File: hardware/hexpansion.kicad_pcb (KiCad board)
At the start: 2 copper layers, 86.8 x 46 mm, 97 parts, among them J1 Hexpansion-Connector, J2 Conn_01x03_Pin, SW1 SKTAACE010, SW2 SKTAACE010, U1 MT3608, U10 XL-0807RGBC-WS2812B-S, U11 XL-0807RGBC-WS2812B-S, U12 XL-0807RGBC-WS2812B-S, U13 XL-0807RGBC-WS2812B-S, U14 XL-0807RGBC-WS2812B-S, U15 XL-0807RGBC-WS2812B-S, U16 XL-0807RGBC-WS2812B-S, U17 XL-0807RGBC-WS2812B-S, U18 XL-0807RGBC-WS2812B-S, U19 XL-0807RGBC-WS2812B-S, U2 ZD24C64A-XGMT, U20 XL-0807RGBC-WS2812B-S, U21 XL-0807RGBC-WS2812B-S, U22 XL-0807RGBC-WS2812B-S, U23 XL-0807RGBC-WS2812B-S, U24 XL-0807RGBC-WS2812B-S, U25 XL-0807RGBC-WS2812B-S, U26 XL-0807RGBC-WS2812B-S, U27 XL-0807RGBC-WS2812B-S, U28 XL-0807RGBC-WS2812B-S, U29 XL-0807RGBC-WS2812B-S, U3 XL-0807RGBC-WS2812B-S, U30 XL-0807RGBC-WS2812B-S, U31 XL-0807RGBC-WS2812B-S, U32 XL-0807RGBC-WS2812B-S, U33 XL-0807RGBC-WS2812B-S, U34 XL-0807RGBC-WS2812B-S, U35 XL-0807RGBC-WS2812B-S, U36 XL-0807RGBC-WS2812B-S, U37 XL-0807RGBC-WS2812B-S, U38 XL-0807RGBC-WS2812B-S, U39 XL-0807RGBC-WS2812B-S, U4 XL-0807RGBC-WS2812B-S, U40 XL-0807RGBC-WS2812B-S, U41 XL-0807RGBC-WS2812B-S, U42 XL-0807RGBC-WS2812B-S, U43 XL-0807RGBC-WS2812B-S, U44 XL-0807RGBC-WS2812B-S, U45 XL-0807RGBC-WS2812B-S, U46 XL-0807RGBC-WS2812B-S, U47 XL-0807RGBC-WS2812B-S, U48 XL-0807RGBC-WS2812B-S, U49 XL-0807RGBC-WS2812B-S, U5 XL-0807RGBC-WS2812B-S, U50 XL-0807RGBC-WS2812B-S, U51 XL-0807RGBC-WS2812B-S, U52 XL-0807RGBC-WS2812B-S, U53 XL-0807RGBC-WS2812B-S, U54 XL-0807RGBC-WS2812B-S, U55 XL-0807RGBC-WS2812B-S, U56 XL-0807RGBC-WS2812B-S, U57 XL-0807RGBC-WS2812B-S, U58 XL-0807RGBC-WS2812B-S, U59 XL-0807RGBC-WS2812B-S, U6 XL-0807RGBC-WS2812B-S, U60 XL-0807RGBC-WS2812B-S, U61 XL-0807RGBC-WS2812B-S, U62 XL-0807RGBC-WS2812B-S, U63 XL-0807RGBC-WS2812B-S, U64 XL-0807RGBC-WS2812B-S, U65 XL-0807RGBC-WS2812B-S, U66 XL-0807RGBC-WS2812B-S, U67 XL-0807RGBC-WS2812B-S, U68 XL-0807RGBC-WS2812B-S, U69 XL-0807RGBC-WS2812B-S, U7 XL-0807RGBC-WS2812B-S, U70 XL-0807RGBC-WS2812B-S, U71 XL-0807RGBC-WS2812B-S, U72 XL-0807RGBC-WS2812B-S, U73 XL-0807RGBC-WS2812B-S, U74 XL-0807RGBC-WS2812B-S, U75 XL-0807RGBC-WS2812B-S, U76 XL-0807RGBC-WS2812B-S, U77 XL-0807RGBC-WS2812B-S, U78 XL-0807RGBC-WS2812B-S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

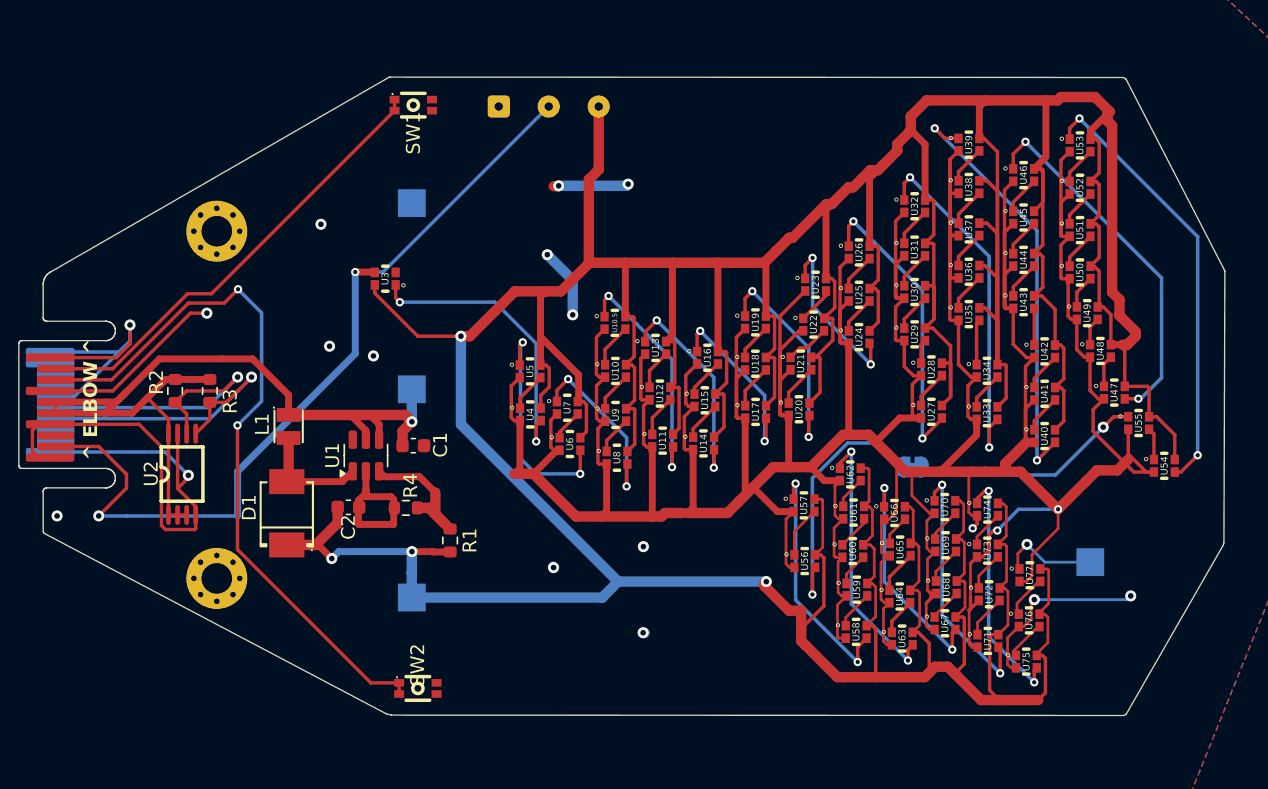
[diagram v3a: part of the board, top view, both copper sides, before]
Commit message: Update silkscreen and add some more ground ties
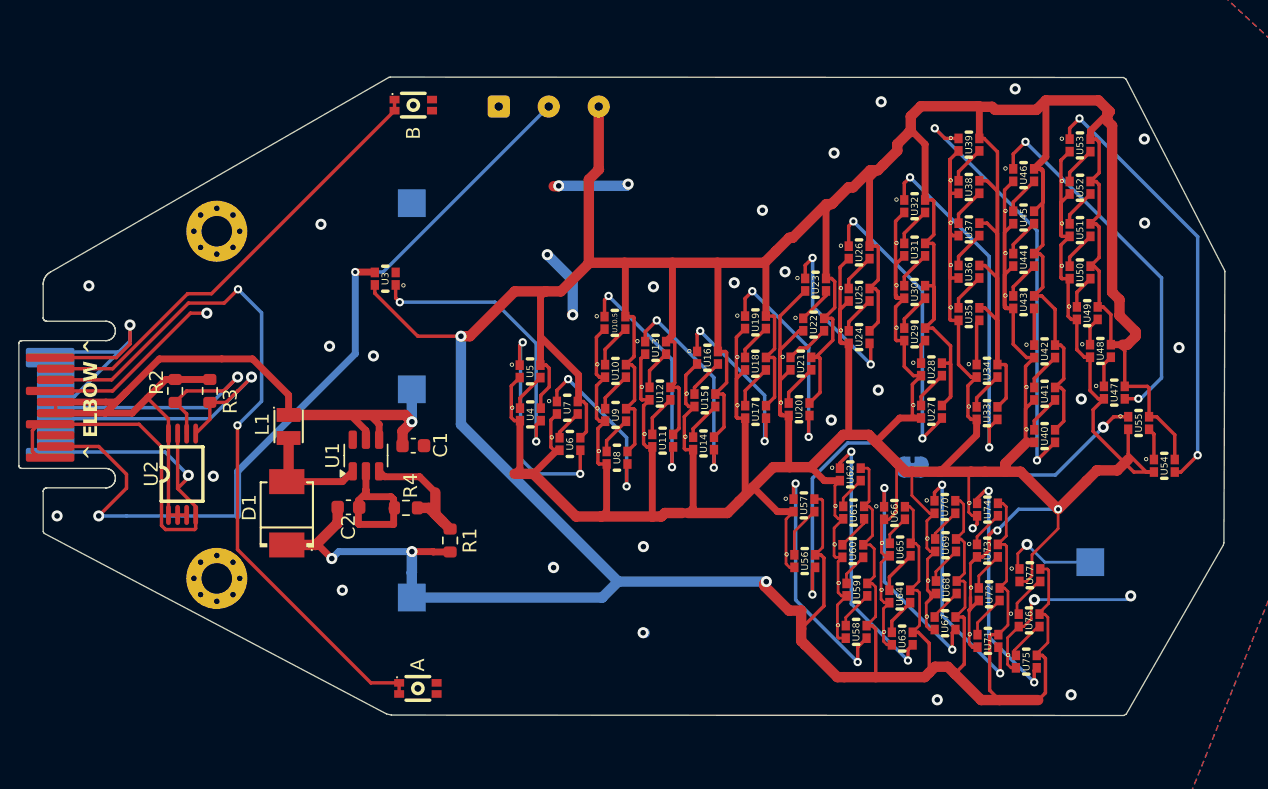
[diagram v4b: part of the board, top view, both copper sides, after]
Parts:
- Data Out: renamed from TP3
- renumbered TP1 to 3.3V, TP2 to 5V, SW2 to A, SW1 to B, TP4 to GND
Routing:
- net +5V: track 541.6 -> 541.0 mm
- net /GND: vias 19 -> 37
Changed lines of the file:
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@@
 		(layer "F.Cu")
 		(at 126.98 120.42)
-		(property "Reference" "SW2"
+		(property "Reference" "A"
 			(at -0.01 -1.69 90)
 			(layer "F.SilkS")
@@
 		(layer "F.Cu")
 		(at 126.65 78.42)
-		(property "Reference" "SW1"
+		(property "Reference" "B"
 			(at 0.01 2.01 90)
 			(layer "F.SilkS")
@@
 		(descr "SMD rectangular pad as test Point, square 2.0mm side length")
 		(tags "test point SMD pad rectangle square")
-		(property "Reference" "TP4"
+		(property "Reference" "GND"
 			(at 0 1.998 90)
 			(layer "B.SilkS")
@@
 		(descr "SMD rectangular pad as test Point, square 2.0mm side length")
 		(tags "test point SMD pad rectangle square")
-		(property "Reference" "TP1"
+		(property "Reference" "3.3V"
 			(at 0 1.998 90)
 			(layer "B.SilkS")
@@
 		(descr "SMD rectangular pad as test Point, square 2.0mm side length")
 		(tags "test point SMD pad rectangle square")
-		(property "Reference" "TP2"
+		(property "Reference" "5V"
 			(at 0 1.998 90)
 			(layer "B.SilkS")
@@
 		(descr "SMD rectangular pad as test Point, square 2.0mm side length")
 		(tags "test point SMD pad rectangle square")
-		(property "Reference" "TP3"
+		(property "Reference" "Data Out"
 			(at 0 1.998 90)
 			(layer "B.SilkS")
@@
 	)
 	(via
+		(at 151.79 85.99)
+		(size 0.8)
+		(drill 0.4)
+		(layers "F.Cu" "B.Cu")
+		(free yes)
+		(net 1)
+	)
+	(via
 		(at 173.08 107.52)
 		(size 0.6)
@@
 	)
 	(via
+		(at 103.29 91.43)
+		(size 0.8)
+		(drill 0.4)
+		(layers "F.Cu" "B.Cu")
+		(free yes)
+		(net 1)
+	)
+	(via
+		(at 149.76 91.21)
+		(size 0.8)
+		(drill 0.4)
+		(layers "F.Cu" "B.Cu")
+		(free yes)
+		(net 1)
+	)
+	(via
 		(at 120 87)
 		(size 0.8)
@@
 	)
 	(via
+		(at 156.75 101.1)
+		(size 0.8)
+		(drill 0.4)
+		(layers "F.Cu" "B.Cu")
+		(free yes)
+		(net 1)
+	)
+	(via
+		(at 156.95 81.87)
+		(size 0.8)
+		(drill 0.4)
+		(layers "F.Cu" "B.Cu")
+		(free yes)
+		(net 1)
+	)
+	(via
+		(at 174.02 120.88)
+		(size 0.8)
+		(drill 0.4)
+		(layers "F.Cu" "B.Cu")
+		(free yes)
+		(net 1)
+	)
+	(via
+		(at 179.29 80.86)
+		(size 0.8)
+		(drill 0.4)
+		(layers "F.Cu" "B.Cu")
+		(free yes)
+		(net 1)
+	)
+	(via
+		(at 169.99 77.25)
+		(size 0.8)
+		(drill 0.4)
+		(layers "F.Cu" "B.Cu")
+		(free yes)
+		(net 1)
+	)
+	(via
+		(at 143.94 91.5)
+		(size 0.8)
+		(drill 0.4)
+		(layers "F.Cu" "B.Cu")
+		(free yes)
+		(net 1)
+	)
+	(via
 		(at 136.3 89.19)
 		(size 0.8)
@@
 	)
 	(via
+		(at 174.75 99.58)
+		(size 0.8)
+		(drill 0.4)
+		(layers "F.Cu" "B.Cu")
+		(free yes)
+		(net 1)
+	)
+	(via
+		(at 121.54 113.35)
+		(size 0.8)
+		(drill 0.4)
+		(layers "F.Cu" "B.Cu")
+		(free yes)
+		(net 1)
+	)
+	(via
+		(at 160.13 98.94)
+		(size 0.8)
+		(drill 0.4)
+		(layers "F.Cu" "B.Cu")
+		(free yes)
+		(net 1)
+	)
+	(via
 		(at 166.93 108.89)
 		(size 0.6)
@@
 	)
 	(via
+		(at 179.31 86.91)
+		(size 0.8)
+		(drill 0.4)
+		(layers "F.Cu" "B.Cu")
+		(free yes)
+		(net 1)
+	)
+	(via
 		(at 168.705 109.05)
 		(size 0.6)
@@
 	)
 	(via
+		(at 153.42 90.42)
+		(size 0.8)
+		(drill 0.4)
+		(layers "F.Cu" "B.Cu")
+		(free yes)
+		(net 1)
+	)
+	(via
+		(at 112.25 105.14)
+		(size 0.8)
+		(drill 0.4)
+		(layers "F.Cu" "B.Cu")
+		(free yes)
+		(net 1)
+	)
+	(via
 		(at 111.785214 93.40067)
 		(size 0.8)
@@
 	)
 	(via
+		(at 181.79 95.88)
+		(size 0.8)
+		(drill 0.4)
+		(layers "F.Cu" "B.Cu")
+		(free yes)
+		(net 1)
+	)
+	(via
+		(at 160.34 78.18)
+		(size 0.8)
+		(drill 0.4)
+		(layers "F.Cu" "B.Cu")
+		(free yes)
+		(net 1)
+	)
+	(via
+		(at 164.38 121.24)
+		(size 0.8)
+		(drill 0.4)
+		(layers "F.Cu" "B.Cu")
+		(free yes)
+		(net 1)
+	)
+	(via
 		(at 123.78 96.48)
 		(size 0.8)
@@
 	)
 	(segment
+		(start 162.47 79.23)
+		(end 162.47 80.26)
+		(width 0.75)
+		(layer "F.Cu")
+		(net 12)
+	)
+	(segment
 		(start 164.0525 91.425)
 		(end 163.5025 91.425)
@@
 	)
 	(segment
-		(start 162.47 80.26)
-		(end 162.47 79.23)
-		(width 0.75)
-		(layer "F.Cu")
-		(net 12)
-	)
-	(segment
 		(start 162.43 113.35)
 		(end 163.061 112.719)
@@
 	)
 	(segment
+		(start 163.2 78.5)
+		(end 162.47 79.23)
+		(width 0.75)
+		(layer "F.Cu")
+		(net 12)
+	)
+	(segment
 		(start 159.55 110.08)
 		(end 159.05 110.08)
@@
 	)
 	(segment
-		(start 173.29 77.84)
-		(end 175.75 77.84)
-		(width 0.75)
-		(layer "F.Cu")
-		(net 12)
-	)
-	(segment
 		(start 119.625 110.09)
 		(end 121.145 108.57)
@@
 	)
 	(segment
-		(start 162.3 80.43)
-		(end 162.47 80.26)
-		(width 0.75)
-		(layer "F.Cu")
-		(net 12)
-	)
-	(segment
 		(start 176.035834 81.091334)
 		(end 176.035834 83.291334)
@@
 	)
 	(segment
+		(start 171.52 78.76)
+		(end 172.2 78.08)
+		(width 0.75)
+		(layer "F.Cu")
+		(net 12)
+	)
+	(segment
 		(start 145.786 98.816)
 		(end 145.71 98.74)
@@
 	)
 	(segment
-		(start 163.62 78.08)
-		(end 167.87 78.08)
-		(width 0.75)
-		(layer "F.Cu")
-		(net 12)
-	)
-	(segment
 		(start 166.281 107.159)
 		(end 166.032 106.91)
@@
 	)
 	(segment
+		(start 167.409834 78.540166)
+		(end 167.369668 78.5)
+		(width 0.75)
+		(layer "F.Cu")
+		(net 12)
+	)
+	(segment
 		(start 168.7125 97.1)
 		(end 168.7125 87.67)
@@
 	)
 	(segment
-		(start 162.47 79.23)
-		(end 163.62 78.08)
-		(width 0.75)
-		(layer "F.Cu")
-		(net 12)
-	)
-	(segment
 		(start 176.035834 89.391334)
 		(end 175.409834 90.017334)
@@
 	)
 	(segment
-		(start 172.2 78.08)
-		(end 173.05 78.08)
-		(width 0.75)
-		(layer "F.Cu")
-		(net 12)
-	)
-	(segment
 		(start 176.035834 84.141334)
 		(end 176.035834 86.341334)
@@
 	)
 	(segment
+		(start 168.55 78.76)
+		(end 171.52 78.76)
+		(width 0.75)
+		(layer "F.Cu")
+		(net 12)
+	)
+	(segment
 		(start 159.692 112.86)
 		(end 159.34 112.86)
@@
 	)
 	(segment
-		(start 173.05 78.08)
-		(end 173.29 77.84)
-		(width 0.75)
-		(layer "F.Cu")
-		(net 12)
-	)
-	(segment
 		(start 171.9 83.01)
 		(end 171.976 83.086)
@@
 	)
 	(segment
-		(start 175.75 77.84)
-		(end 176.8 78.89)
+		(start 167.409834 78.540166)
+		(end 168.330166 78.540166)
 		(width 0.75)
 		(layer "F.Cu")
@@
 	)
 	(segment
+		(start 162.47 80.26)
+		(end 162.3 80.43)
+		(width 0.75)
+		(layer "F.Cu")
+		(net 12)
+	)
+	(segment
 		(start 173.4885 101.174)
 		(end 172.8625 101.8)
@@
 	)
 	(segment
+		(start 167.409834 78.540166)
+		(end 167.409834 80.817334)
+		(width 0.5)
+		(layer "F.Cu")
+		(net 12)
+	)
+	(segment
 		(start 152.59 93.61)
 		(end 152.04 93.61)
@@
 	)
 	(segment
-		(start 167.87 78.08)
-		(end 172.2 78.08)
-		(width 0.75)
-		(layer "F.Cu")
-		(net 12)
-	)
-	(segment
 		(start 128.085 110.595)
 		(end 129.3 110.595)
@@
 	)
 	(segment
+		(start 172.2 78.08)
+		(end 175.99 78.08)
+		(width 0.75)
+		(layer "F.Cu")
+		(net 12)
+	)
+	(segment
 		(start 168.7125 97.1)
 		(end 168.7125 90.868)
@@
 	)
 	(segment
+		(start 168.330166 78.540166)
+		(end 168.55 78.76)
+		(width 0.75)
+		(layer "F.Cu")
+		(net 12)
+	)
+	(segment
 		(start 164.0525 94.475)
 		(end 163.5025 94.475)
@@
 	)
 	(segment
-		(start 167.409834 78.540166)
-		(end 167.87 78.08)
-		(width 0.5)
-		(layer "F.Cu")
-		(net 12)
-	)
-	(segment
 		(start 175.409834 90.017334)
 		(end 175.682666 90.017334)
@@
 	)
 	(segment
-		(start 167.409834 80.817334)
-		(end 167.409834 78.540166)
-		(width 0.5)
+		(start 167.369668 78.5)
+		(end 163.2 78.5)
+		(width 0.75)
 		(layer "F.Cu")
 		(net 12)
@@
 		(layer "F.Cu")
 		(net 12)
+	)
+	(segment
+		(start 175.99 78.08)
+		(end 176.8 78.89)
+		(width 0.75)
+		(layer "F.Cu")
+		(net 12)

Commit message: Ready to fab
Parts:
- added G***: LOGO, LOGO, F.Cu at (174.7, 104.3)
- added G***: LOGO, LOGO, F.Cu at (130.6, 91.5)
- added G***: LOGO, LOGO, F.Cu at (147.9, 114.3)
- added G***: LOGO, LOGO, F.Cu at (146.5, 118.9)
- added G***: LOGO, LOGO, F.Cu at (181.8, 110.4)
- added G***: LOGO, LOGO, F.Cu at (165.9, 103.3)
- added G***: LOGO, LOGO, F.Cu at (140.8, 82.5)
- added G***: LOGO, LOGO, F.Cu at (138.8, 111.2)
- added G***: LOGO, LOGO, F.Cu at (151.4, 117.3)
- added G***: LOGO, LOGO, F.Cu at (138.0, 85.7)
- added G***: LOGO, LOGO, F.Cu at (135.4, 118.7)
- added G***: LOGO, LOGO, F.Cu at (150.1, 85.7)
- added G***: LOGO, LOGO, F.Cu at (149.8, 79.5)
- added G***: LOGO, LOGO, F.Cu at (145.5, 86.5)
- added G***: LOGO, LOGO, F.Cu at (153.5, 81.5)
- added G***: LOGO, LOGO, F.Cu at (175.1, 113.6)
- added G***: LOGO, LOGO, F.Cu at (150.8, 109.4)
- added G***: LOGO, LOGO, F.Cu at (177.1, 117.3)
- added G***: LOGO, LOGO, F.Cu at (130.1, 101.6)
- added G***: LOGO, LOGO, F.Cu at (180.5, 91.4)
- added G***: LOGO, LOGO, F.Cu at (129.4, 82.8)
- added G***: LOGO, LOGO, F.Cu at (177.5, 108.4)
- added G***: LOGO, LOGO, F.Cu at (132.5, 86.3)
- added G***: LOGO, LOGO, F.Cu at (122.8, 82.5)
- added G***: LOGO, LOGO, F.Cu at (180.6, 84.4)
- added G***: LOGO, LOGO, F.Cu at (147.2, 90.1)
- added G***: LOGO, LOGO, F.Cu at (140.5, 117.4)
- added G***: LOGO, LOGO, B.Cu at (161.5, 102.2)
- added G***: LOGO, LOGO, F.Cu at (158.8, 100.5)
- added G***: LOGO, LOGO, F.Cu at (144.9, 81.5)
- added G***: LOGO, LOGO, F.Cu at (134.3, 109.4)
- added G***: LOGO, LOGO, F.Cu at (146.0, 110.5)
- added G***: LOGO, LOGO, F.Cu at (183.0, 95.4)
- added G***: LOGO, LOGO, F.Cu at (158.5, 80.5)
- 5V | Data | GND: renamed from J2
- R1: value 750k -> 750K
- R4: value 100k -> 100K
- moved L1 1.62 mm to (119.3, 101.6)
- moved D1 0.91 mm to (118.3, 107.3)
- moved C1 0.62 mm to (126.2, 103.3), turned to -90 degrees
- renumbered JP1 to J1
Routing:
- net /GND: track 505.0 -> 512.5 mm, vias 37 -> 38
- net /3V3: track 74.2 -> 69.8 mm
- net /HS_I: track 61.1 -> 57.0 mm
- net Net-(U1-FB): track 10.4 -> 9.82 mm, vias 0 -> 2
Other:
- board size 86.8 x 46 mm -> 88 x 46 mm
